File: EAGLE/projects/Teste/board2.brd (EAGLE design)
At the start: 100 x 80 mm, 21 parts, among them IC1 317T, IC2 7805T

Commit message: Placa Roteada
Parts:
- moved R5 10.8 mm to (26.0, 69.1), turned to 180 degrees
- moved C1 6.85 mm to (80.6, 64.8)
- moved R1 6.85 mm to (78.4, 60.7)
- moved C2 3.38 mm to (83.3, 51.2)
- moved JP3 3.38 mm to (89.2, 51.2)
- moved C4 3.38 mm to (77.1, 50.7)
- moved JP1 2.68 mm to (12.7, 64.3)
- moved DIS1 1.67 mm to (40.3, 91.4)
- moved R6 0.18 mm to (3.43, 65.2), turned to 90 degrees
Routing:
- net N$3: track 58.2 -> 129.5 mm
- net +5V: track 224.2 -> 272.5 mm, vias 0 -> 4
- net LCD_RS: track 0.00 -> 39.0 mm
- net 3V: track 33.2 -> 50.6 mm
- net DATA_DHT: track 35.0 -> 18.3 mm
- net N$6: track 4.46 -> 19.9 mm
- net +3V3: track 48.4 -> 38.5 mm
- net N$1: track 11.7 -> 17.4 mm
- net LCD_D7: track 34.4 -> 31.4 mm
- net GND: track 387.3 -> 390.2 mm
- net LCD_E: track 39.2 -> 36.5 mm
- net LCD_D6: track 33.8 -> 31.4 mm
- net N$5: track 46.8 -> 45.0 mm
- net LCD_D4: track 29.4 -> 27.8 mm
- net LCD_D5: track 29.4 -> 27.8 mm

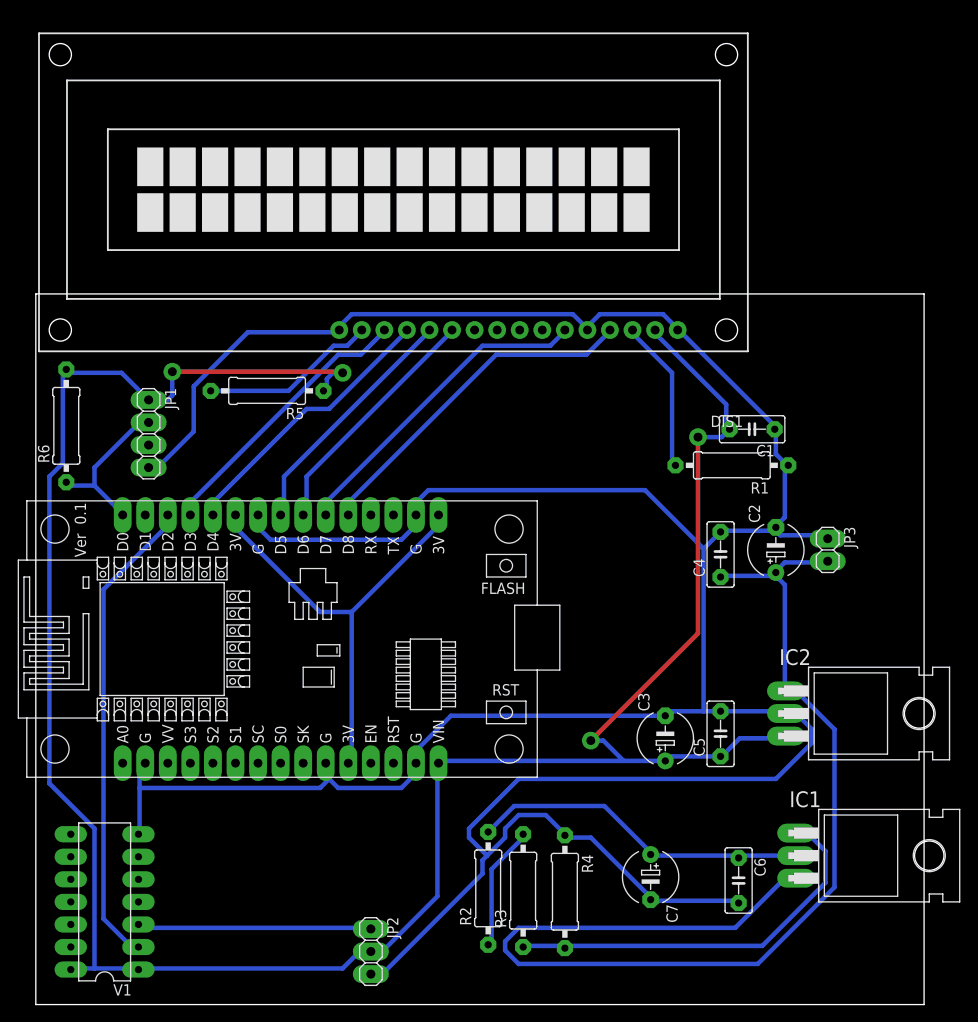
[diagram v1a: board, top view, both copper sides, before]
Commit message: Roteamento em 30mils
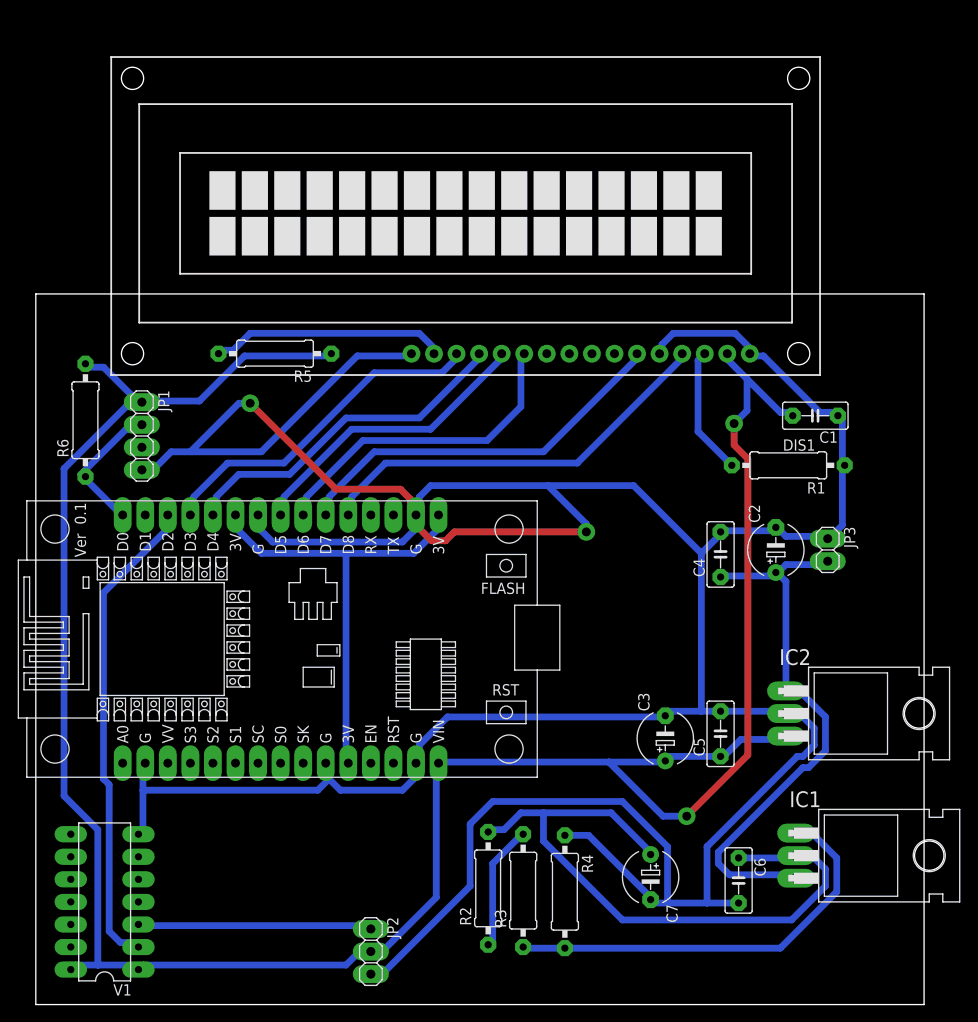
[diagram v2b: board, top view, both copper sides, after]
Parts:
- moved DIS1 8.55 mm to (48.4, 88.8)
- moved C1 7.27 mm to (87.8, 66.3)
- moved R1 6.35 mm to (84.7, 60.7)
- moved R5 4.28 mm to (26.9, 73.3)
- moved R6 2.25 mm to (5.59, 65.8)
- moved JP1 0.80 mm to (11.9, 64.0)
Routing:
- net N$3: track 129.5 -> 63.9 mm
- net GND: track 390.2 -> 430.4 mm, vias 0 -> 2
- net +3V3: track 38.5 -> 73.8 mm
- net LCD_D4: track 27.8 -> 36.8 mm
- net LCD_RS: track 39.0 -> 46.7 mm
- net LCD_D7: track 31.4 -> 39.1 mm
- net LCD_D6: track 31.4 -> 39.1 mm
- net LCD_E: track 36.5 -> 44.2 mm
- net N$6: track 19.9 -> 26.7 mm
- net LCD_D5: track 27.8 -> 34.0 mm
- net +5V: track 272.5 -> 277.8 mm, vias 4 -> 2
- net N$1: track 17.4 -> 14.5 mm
- net N$5: track 45.0 -> 47.5 mm
- net DATA_DHT: track 18.3 -> 15.8 mm
- net 3V: track 50.6 -> 51.9 mm
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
